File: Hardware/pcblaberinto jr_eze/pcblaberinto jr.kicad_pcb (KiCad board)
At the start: 2 copper layers, 20 parts, among them J1 Ultrasonido, J2 Ultrasonido, J3 Ultrasonido, J4 CableAlimentacion, J5 Jumper, J7 EncoderMotorDerecha, J8 EncoderMotorIzquierda, J9 Input of Driver L9110, SW1 SW_Push, U1 L7805

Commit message: modificaciones a la placa
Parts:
- J1: moved to F.Cu
- moved H1 75.5 mm to (122.5, 74.0)
- moved H2 66.5 mm to (198.5, 119.0)
- moved J8 33.5 mm to (126.5, 99.0), turned to 90 degrees
- moved J7 21.7 mm to (126.5, 88.0), turned to 90 degrees
- moved J9 19.0 mm to (157.1, 75.9)
- moved SW1 6.12 mm to (127.7, 73.8)
- moved J3 5.35 mm to (145.7, 114.6)
- moved J2 5.11 mm to (158.5, 114.6)
- moved J1 4.87 mm to (171.3, 114.6)
- moved UM1 3.33 mm to (159.5, 93.5)
- moved ? 1.41 mm to (187.3, 112.3)
- moved C1 1.41 mm to (191.4, 79.2)
- moved C2 1.41 mm to (191.4, 82.7)
- moved C3 1.41 mm to (194.4, 94.7)
- moved C4 1.41 mm to (194.4, 91.7)
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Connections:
- J9 pad 5: /IN4 -> /IN3
- J9 pad 6: /IN3 -> /IN4
- UM1 pad 8: /ECCHO_1 -> unconnected-(UM1-Pad8)
- UM1 pad 9: /TRIGG_1 -> /ECCHO_1
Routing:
- net /IN3: track 34.5 -> 5.50 mm
- net /D0B: track 4.74 -> 33.2 mm
- net /TRIGG_1: track 18.4 -> 41.0 mm
- net /IN4: track 26.1 -> 5.50 mm
- net GND: track 206.1 -> 226.2 mm, vias 0 -> 2
- net +7.5V: track 32.2 -> 51.7 mm
- net /ECCHO_1: track 14.2 -> 31.7 mm
- net /IN2: track 21.1 -> 5.40 mm
- net /IN1: track 19.9 -> 5.40 mm
- net /D0: track 6.82 -> 18.6 mm
- net +5V: track 163.2 -> 169.6 mm
- net /TRIGG_2: track 17.8 -> 12.8 mm
- net /BOTON: track 11.2 -> 13.5 mm
- net /TRIGG_3: track 13.4 -> 14.7 mm
- net /ECCHO_2: track 10.0 -> 9.37 mm

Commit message: cambios en la placa para que los corrija tashe
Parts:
- LED1: footprint LED_SMD:LED_1206_3216Metric -> EESTN5:led_3mm_red; moved to F.Cu
- moved SW1 2.43 mm to (127.4, 76.2)
- moved LED1 0.50 mm to (192.4, 99.0), turned to 0 degrees
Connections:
- J1 pad 2: /TRIGG_1 -> GND
- J1 pad 4: GND -> /TRIGG_1
- UM1 pad 10: /TRIGG_1 -> /ECCHO_1
- UM1 pad 9: /ECCHO_1 -> /TRIGG_1
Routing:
- net /TRIGG_1: track 41.0 -> 12.2 mm
- net /ECCHO_1: track 31.7 -> 15.6 mm
- net +5V: track 169.6 -> 166.1 mm
- net GND: track 226.2 -> 228.6 mm, vias 2 -> 0
- net /BOTON: track 13.5 -> 11.8 mm
- net Net-(R1-Pad1): track 3.25 -> 3.81 mm

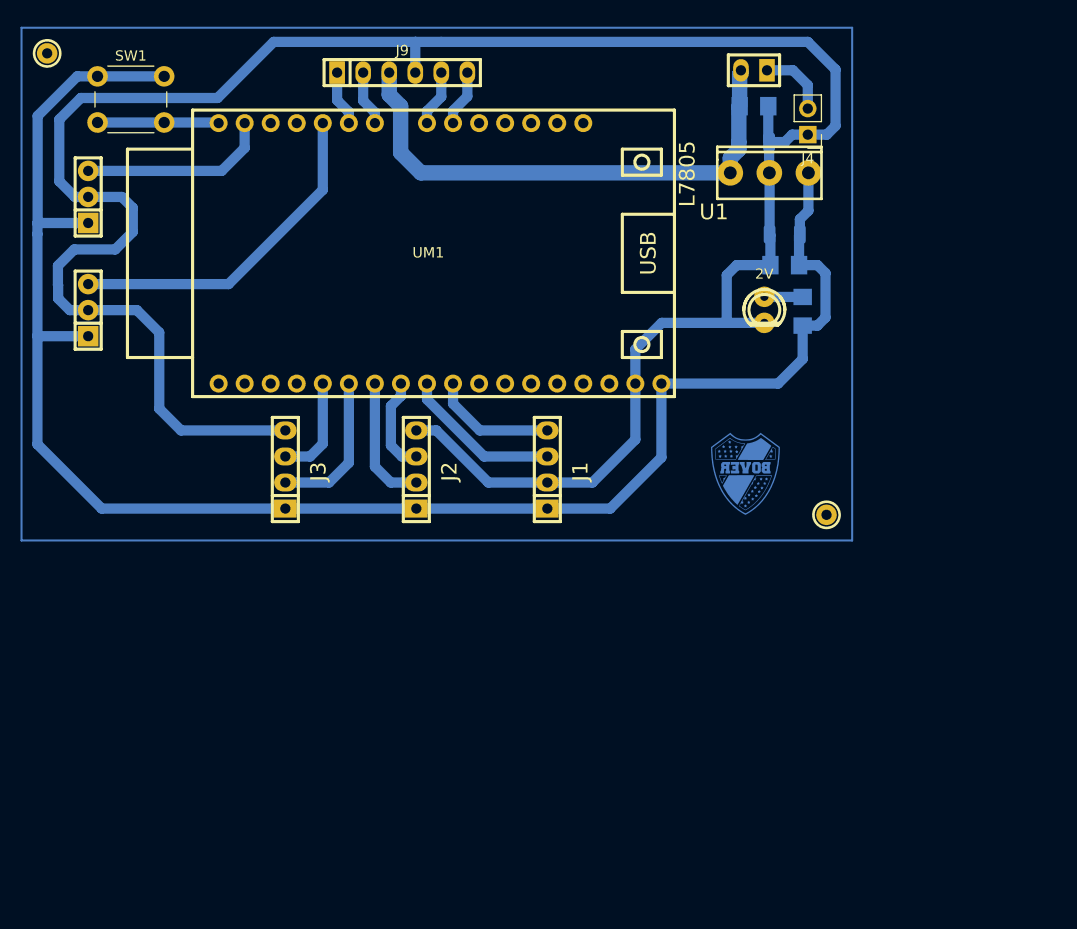
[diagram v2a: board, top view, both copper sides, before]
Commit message: agregando la placa de bover ORIGIN Y ORDENANDO UN POCO
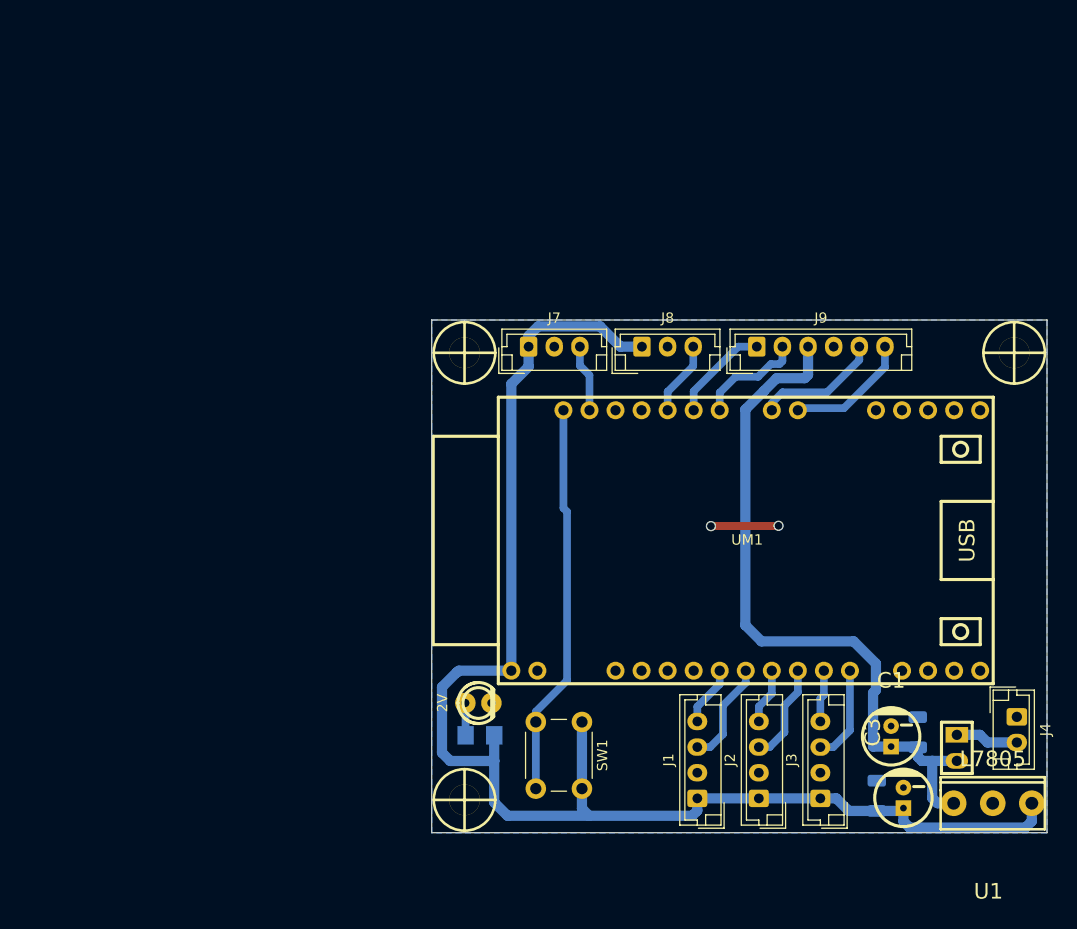
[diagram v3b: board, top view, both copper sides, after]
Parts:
- removed ?: , clipboard:f8367c0e-1178-412a-9d09-4bd76832e1de
- removed H2: Mounting_Hole, EESTN5:pad_2mm
- added H3: Mounting_Hole, EESTN5:hole_3mm, F.Cu at (216.8, 103.2)
- added H4: Mounting_Hole, EESTN5:hole_3mm, F.Cu at (163.2, 103.2)
- C1, C3: footprint EESTN5:C_1206 -> EESTN5:CAP_ELEC_5x11mm; moved to F.Cu
- H1: footprint EESTN5:pad_2mm -> EESTN5:hole_3mm
- J1, J2, J3: footprint EESTN5:pin_strip_4 -> Connector_JST:JST_EH_B4B-EH-A_1x04_P2.50mm_Vertical
- J4: footprint Connector_PinHeader_2.54mm:PinHeader_1x02_P2.54mm_Vertical -> Connector_JST:JST_EH_B2B-EH-A_1x02_P2.50mm_Vertical
- J5: footprint EESTN522:Jumper -> EESTN5:Jumper
- J7, J8: footprint EESTN5:Pin_Strip_3 -> Connector_JST:JST_EH_B3B-EH-A_1x03_P2.50mm_Vertical
- J9: footprint EESTN5:Pin_Header_6 -> Connector_JST:JST_EH_B6B-EH-A_1x06_P2.50mm_Vertical
- moved H1 83.4 mm to (163.2, 146.8)
- moved SW1 78.7 mm to (174.7, 139.2), turned to -90 degrees
- moved J5 69.0 mm to (211.2, 141.7), turned to -90 degrees
- moved U1 65.2 mm to (214.7, 147.1)
- moved C1 62.9 mm to (204.8, 140.6), turned to 0 degrees
- moved J3 61.2 mm to (197.9, 146.7)
- moved J4 60.3 mm to (217.1, 138.7), turned to -90 degrees
- moved C2 59.7 mm to (207.4, 140.2), turned to 90 degrees
- moved C4 55.5 mm to (203.4, 146.4), turned to -90 degrees
- moved J8 54.1 mm to (180.5, 102.6), turned to 0 degrees
- moved C3 53.2 mm to (206.0, 146.6)
- moved R1 52.0 mm to (164.7, 140.5), turned to 180 degrees
- moved LED1 47.4 mm to (164.6, 137.3), turned to 90 degrees
- moved J2 46.3 mm to (191.9, 146.7)
- moved J7 45.4 mm to (169.4, 102.6), turned to 0 degrees
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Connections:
- J2 pad 2: /TRIGG_2 -> GND
- J2 pad 3: /ECCHO_2 -> /TRIGG_2
- J2 pad 4: GND -> /ECCHO_2
- J3 pad 2: /TRIGG_3 -> GND
- J3 pad 4: GND -> /TRIGG_3
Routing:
- net GND: track 228.6 -> 6.60 mm, vias 0 -> 2
- net +5V: track 166.1 -> 138.4 mm
- net /BOTON: track 11.8 -> 38.3 mm
- net /D0B: track 33.2 -> 7.23 mm
- net +7.5V: track 51.7 -> 69.0 mm
- net /D0: track 18.6 -> 6.59 mm
- net /TRIGG_3: track 14.7 -> 5.09 mm
- net /IN3: track 5.50 -> 12.3 mm
- net /IN4: track 5.50 -> 12.2 mm
- net /TRIGG_1: track 12.2 -> 5.86 mm
- net /ECCHO_1: track 15.6 -> 10.1 mm
- net /IN2: track 5.40 -> 10.5 mm
- net /IN1: track 5.40 -> 9.80 mm
- net /ECCHO_2: track 9.37 -> 5.47 mm
- net /TRIGG_2: track 12.8 -> 9.64 mm
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- added copper zone on B.Cu, net GND
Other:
- board outline added: 60 x 50 mm

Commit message: prueba encoders
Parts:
- moved SW1 7.53 mm to (170.1, 145.2), turned to 90 degrees
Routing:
- net /BOTON: track 38.3 -> 37.7 mm
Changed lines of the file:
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@@
   )
   (footprint "Button_Switch_THT:SW_PUSH_6mm_H4.3mm" (layer "F.Cu")
-    (at 174.65 139.2 -90)
+    (at 170.13 145.22 90)
     (descr "tactile push button, 6x6mm e.g. PHAP33xx series, height=4.3mm")
     (tags "tact sw push 6mm")
@@
     (fp_line (start 6.25 -0.75) (end 6.25 5.25) (layer "F.Fab") (width 0.1))
     (fp_circle (center 3.25 2.25) (end 1.25 2.5) (layer "F.Fab") (width 0.1) (fill none))
-    (pad "1" thru_hole circle (at 6.5 0) (size 2 2) (drill 1.1) (layers *.Cu *.Mask)
+    (pad "1" thru_hole circle (at 6.5 0 180) (size 2 2) (drill 1.1) (layers *.Cu *.Mask)
       (net 3 "+5V") (pinfunction "1") (pintype "passive"))
-    (pad "1" thru_hole circle (at 0 0) (size 2 2) (drill 1.1) (layers *.Cu *.Mask)
+    (pad "1" thru_hole circle (at 0 0 180) (size 2 2) (drill 1.1) (layers *.Cu *.Mask)
       (net 3 "+5V") (pinfunction "1") (pintype "passive"))
-    (pad "2" thru_hole circle (at 0 4.5) (size 2 2) (drill 1.1) (layers *.Cu *.Mask)
+    (pad "2" thru_hole circle (at 0 4.5 180) (size 2 2) (drill 1.1) (layers *.Cu *.Mask)
       (net 5 "/BOTON") (pinfunction "2") (pintype "passive"))
-    (pad "2" thru_hole circle (at 6.5 4.5) (size 2 2) (drill 1.1) (layers *.Cu *.Mask)
+    (pad "2" thru_hole circle (at 6.5 4.5 180) (size 2 2) (drill 1.1) (layers *.Cu *.Mask)
       (net 5 "/BOTON") (pinfunction "2") (pintype "passive"))
     (model "${KICAD6_3DMODEL_DIR}/Button_Switch_THT.3dshapes/SW_PUSH_6mm_H4.3mm.wrl"
@@
   (segment (start 218.52 148.88) (end 218.52 147.125) (width 1) (layer "B.Cu") (net 3))
   (segment (start 166.097 147.047) (end 166.097 143.003) (width 1) (layer "B.Cu") (net 3))
+  (segment (start 170 148.35) (end 167.4 148.35) (width 1) (layer "B.Cu") (net 3))
   (segment (start 197.9 146.65) (end 199.45 146.65) (width 1) (layer "B.Cu") (net 3))
-  (segment (start 175.35 148.35) (end 174.65 147.65) (width 1) (layer "B.Cu") (net 3))
   (segment (start 199.45 146.65) (end 200.675 147.875) (width 1) (layer "B.Cu") (net 3))
+  (segment (start 169.39 140.5) (end 170.11 139.78) (width 1) (layer "B.Cu") (net 3))
   (segment (start 169.45 104.55) (end 167.765 106.235) (width 1) (layer "B.Cu") (net 3))
   (segment (start 169.45 102.6) (end 169.45 104.55) (width 1) (layer "B.Cu") (net 3))
-  (segment (start 174.65 145.7) (end 174.65 140.15) (width 1) (layer "B.Cu") (net 3))
   (segment (start 166.097 143.003) (end 161.803 143.003) (width 1) (layer "B.Cu") (net 3))
   (segment (start 169.45 101.55) (end 170.37452 100.62548) (width 1) (layer "B.Cu") (net 3))
-  (segment (start 174.65 147.65) (end 174.65 145.7) (width 1) (layer "B.Cu") (net 3))
   (segment (start 205.725 147.875) (end 206 147.6) (width 1) (layer "B.Cu") (net 3))
   (segment (start 167.4 148.35) (end 166.097 147.047) (width 1) (layer "B.Cu") (net 3))
@@
   (segment (start 185.9 147.85) (end 185.4 148.35) (width 1) (layer "B.Cu") (net 3))
   (segment (start 170.37452 100.62548) (end 176.42548 100.62548) (width 1) (layer "B.Cu") (net 3))
+  (segment (start 170.13 145.22) (end 170.13 148.22) (width 1) (layer "B.Cu") (net 3))
+  (segment (start 170.11 139.78) (end 170.11 138.74) (width 1) (layer "B.Cu") (net 3))
+  (segment (start 175.35 148.35) (end 170 148.35) (width 1) (layer "B.Cu") (net 3))
   (segment (start 162.45 134.35) (end 162.5 134.35) (width 1) (layer "B.Cu") (net 3))
   (segment (start 185.9 146.65) (end 185.9 147.85) (width 1) (layer "B.Cu") (net 3))
   (segment (start 206 147.6) (end 206 148.89) (width 1) (layer "B.Cu") (net 3))
+  (segment (start 170.13 148.22) (end 170 148.35) (width 1) (layer "B.Cu") (net 3))
   (segment (start 217.90002 149.49998) (end 218.52 148.88) (width 1) (layer "B.Cu") (net 3))
   (segment (start 176.42548 100.62548) (end 178.4 102.6) (width 1) (layer "B.Cu") (net 3))
-  (segment (start 175.35 148.35) (end 167.4 148.35) (width 1) (layer "B.Cu") (net 3))
   (segment (start 200.675 147.875) (end 203.4 147.875) (width 1) (layer "B.Cu") (net 3))
   (segment (start 206 148.89) (end 206.60998 149.49998) (width 1) (layer "B.Cu") (net 3))
   (segment (start 161 142.2) (end 161 135.8) (width 1) (layer "B.Cu") (net 3))
+  (segment (start 170.11 138.74) (end 170.13 138.72) (width 1) (layer "B.Cu") (net 3))
   (segment (start 161.803 143.003) (end 161 142.2) (width 1) (layer "B.Cu") (net 3))
+  (segment (start 166.097 140.5) (end 169.39 140.5) (width 1) (layer "B.Cu") (net 3))
   (segment (start 169.45 102.6) (end 169.45 101.55) (width 1) (layer "B.Cu") (net 3))
   (segment (start 185.4 148.35) (end 175.35 148.35) (width 1) (layer "B.Cu") (net 3))
@@
   (segment (start 214.2 141.2) (end 217.06 141.2) (width 1) (layer "B.Cu") (net 4))
   (segment (start 213.455 140.455) (end 214.2 141.2) (width 1) (layer "B.Cu") (net 4))
-  (segment (start 170.15 139.2) (end 170.15 145.7) (width 0.75) (layer "B.Cu") (net 5))
-  (segment (start 170.15 139.2) (end 170.15 138.2) (width 0.75) (layer "B.Cu") (net 5))
-  (segment (start 170.15 138.2) (end 173.2 135.15) (width 0.75) (layer "B.Cu") (net 5))
-  (segment (start 173.2 135.15) (end 173.2 118.7) (width 0.75) (layer "B.Cu") (net 5))
-  (segment (start 172.845 118.345) (end 172.845 108.8) (width 0.75) (layer "B.Cu") (net 5))
-  (segment (start 173.2 118.7) (end 172.845 118.345) (width 0.75) (layer "B.Cu") (net 5))
+  (segment (start 172.845 118.345) (end 173.2 118.7) (width 0.75) (layer "B.Cu") (net 5))
+  (segment (start 174.6 137.31) (end 174.6 139.24) (width 0.75) (layer "B.Cu") (net 5))
+  (segment (start 172.845 108.8) (end 172.845 118.345) (width 0.75) (layer "B.Cu") (net 5))
+  (segment (start 173.2 135.91) (end 174.6 137.31) (width 0.75) (layer "B.Cu") (net 5))
+  (segment (start 174.6 145.74) (end 174.6 139.24) (width 0.75) (layer "B.Cu") (net 5))
+  (segment (start 173.2 118.7) (end 173.2 135.91) (width 0.75) (layer "B.Cu") (net 5))
   (segment (start 163.303 140.5) (end 163.303 137.373) (width 0.75) (layer "B.Cu") (net 6))
   (segment (start 163.303 137.373) (end 163.28 137.35) (width 0.75) (layer "B.Cu") (net 6))
